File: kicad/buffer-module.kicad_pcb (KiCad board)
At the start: 2 copper layers, 19 x 100 mm, 36 parts, among them J1 Jack_InA, J2 Jack_InB, J3 Jack_OutA-1, J4 Jack_OutA-2, J5 Jack_OutA-3, J6 Jack_OutB-1, J7 Jack_OutB-2, J8 Jack_OutB-3, J9 Conn_02x05_Odd_Even, U1 TL074, U2 TL074

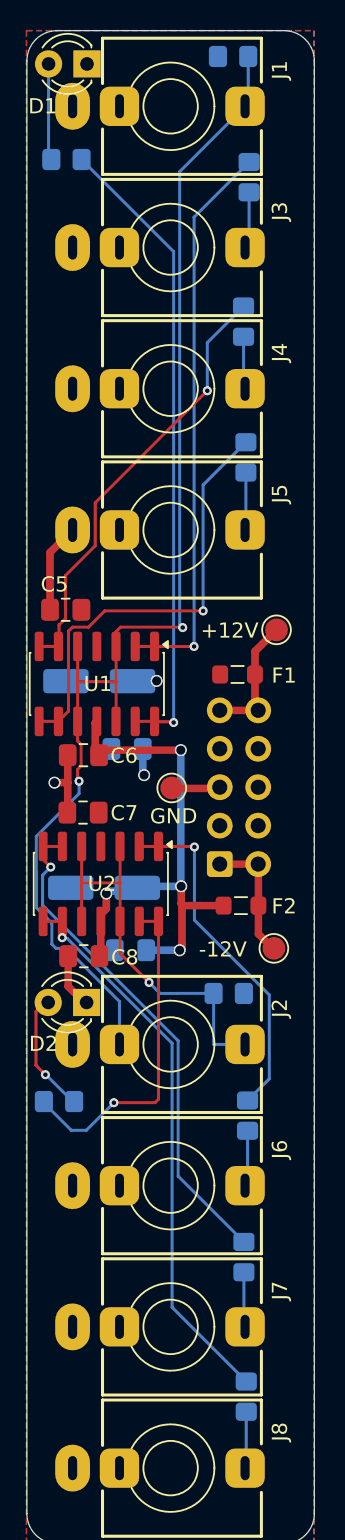
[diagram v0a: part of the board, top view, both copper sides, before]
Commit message: Refactor buffer-module: Remove unused silk layers and update footprint references
- Removed multiple unused silk layer entries from buffer-module.kicad_pro to clean up the design.
- Updated footprint references in buffer-module.kicad_sch from "AudioJacks2" to "Eurorack" for consistency across the schematic.
- Deleted the lock file ~buffer-module.kicad_sch.lck as it is no longer needed.
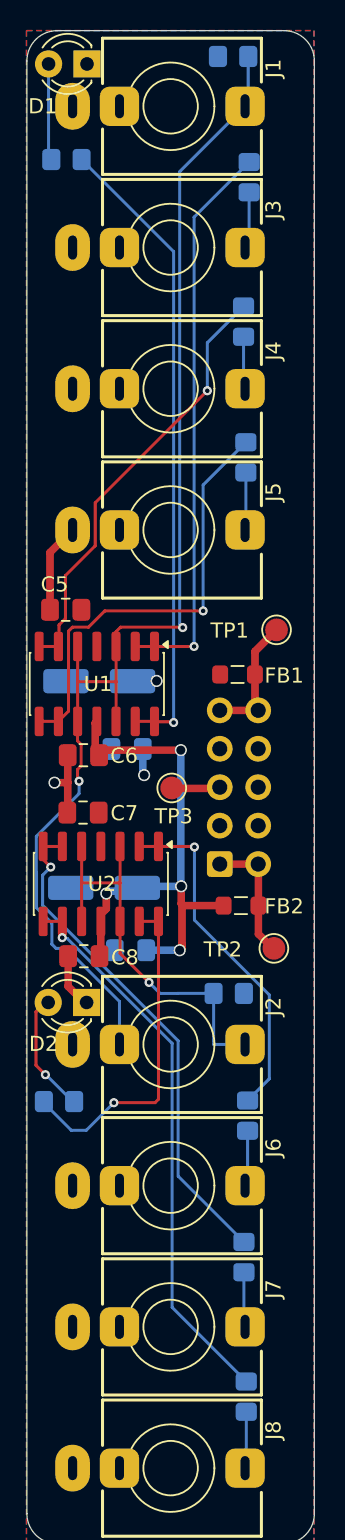
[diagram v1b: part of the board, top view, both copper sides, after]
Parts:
- J1, J2, J3, J4, J5, J6, J7, J8: footprint AudioJacks2:Jack_3.5mm_QingPu_WQP-PJ398SM_Vertical -> Eurorack:Jack_3.5mm_QingPu_WQP-PJ398SM_Vertical
- renumbered F1 to FB1, F2 to FB2, +12V to TP1, -12V to TP2, GND to TP3

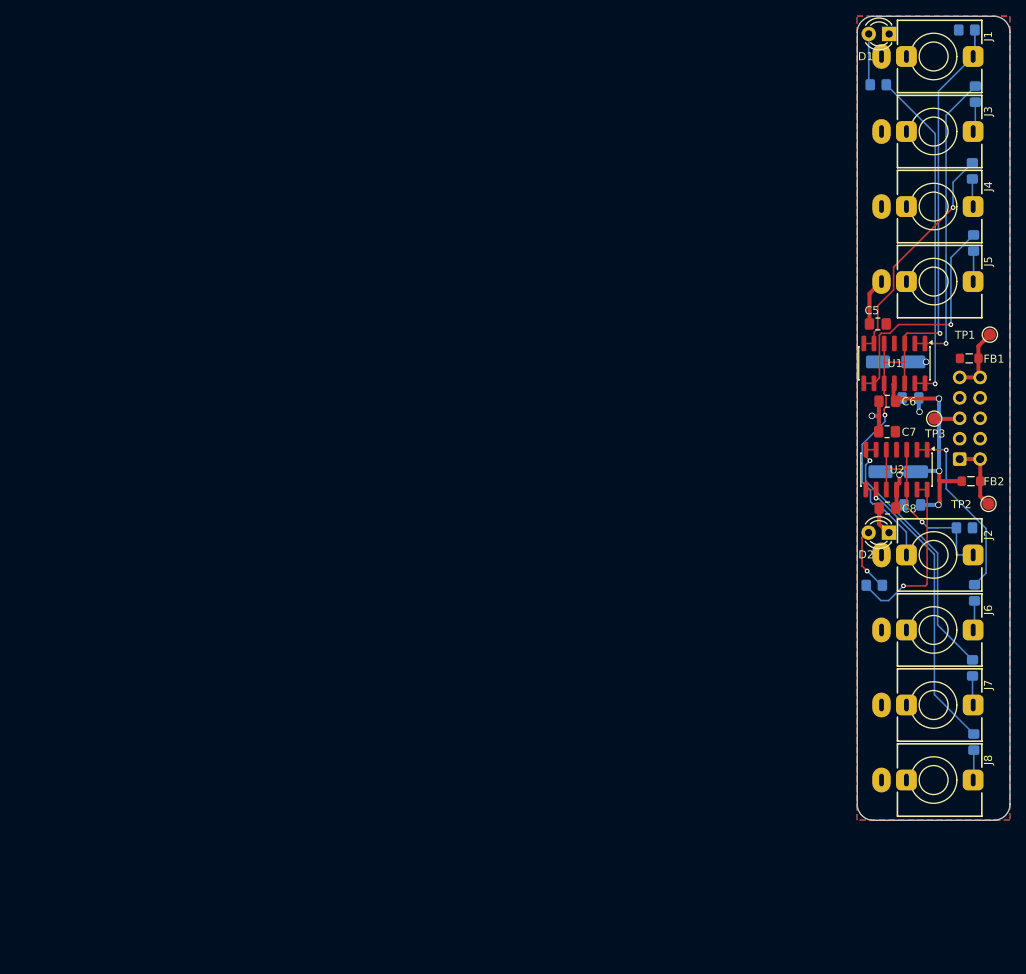
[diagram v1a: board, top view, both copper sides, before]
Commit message: Refactor KiCad project files for improved layout and organization
- Adjusted column widths in buffer-module.kicad_prl for better readability.
- Cleared unnecessary DRC exclusions in buffer-module.kicad_pro to streamline design rules.
- Updated sheet positions and properties in buffer-module.kicad_sch for enhanced clarity.
- Realigned junctions and wires in quad buffer schematic for improved circuit flow and readability.
- Corrected component positions and properties in quad buffer schematic to ensure accurate representation.
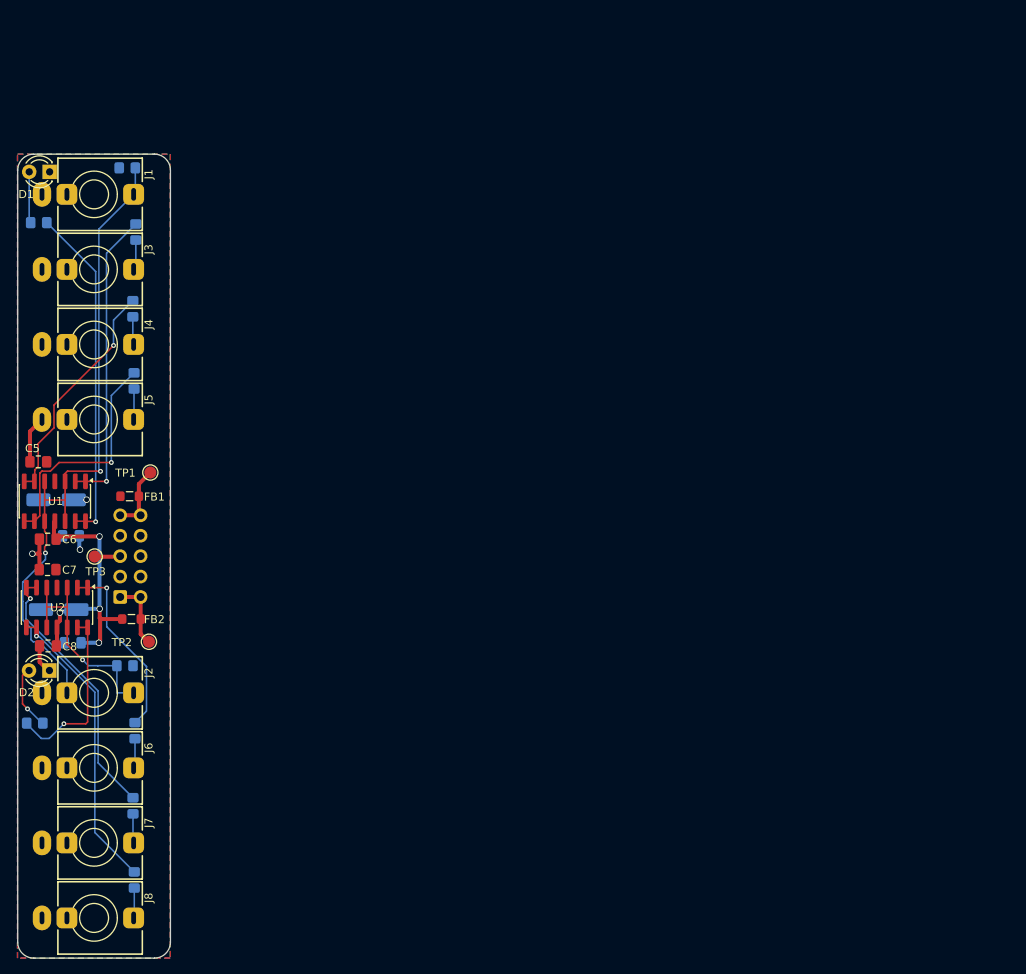
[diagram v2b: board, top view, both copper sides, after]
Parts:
- moved C1 105.8 mm to (90.9, 94.1)
- moved C3 105.8 mm to (92.7, 98.6)
- moved C7 105.8 mm to (89.8, 102.8)
- moved C8 105.8 mm to (89.9, 112.3)
- moved FB2 105.8 mm to (100.2, 109.0)
- moved J9 105.8 mm to (98.8, 106.2)
- moved R10 105.8 mm to (88.2, 121.9)
- moved R2 105.8 mm to (100.8, 60.8)
- moved R3 105.8 mm to (100.4, 70.4)
- moved R5 105.8 mm to (88.7, 59.7)
- moved R9 105.8 mm to (100.6, 141.4)
- moved TP1 105.8 mm to (102.6, 90.8)
- moved U1 105.8 mm to (90.7, 94.3)
- moved C2 105.8 mm to (91.2, 107.8)
- moved C4 105.8 mm to (93.0, 111.9)
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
